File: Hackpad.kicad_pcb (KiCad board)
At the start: 2 copper layers, 21 x 58.5 mm, 4 parts, among them SW1 SW_Push, SW2 SW_Push, SW3 SW_Push, U1 MOUDLE-SEEEDUINO-XIAO

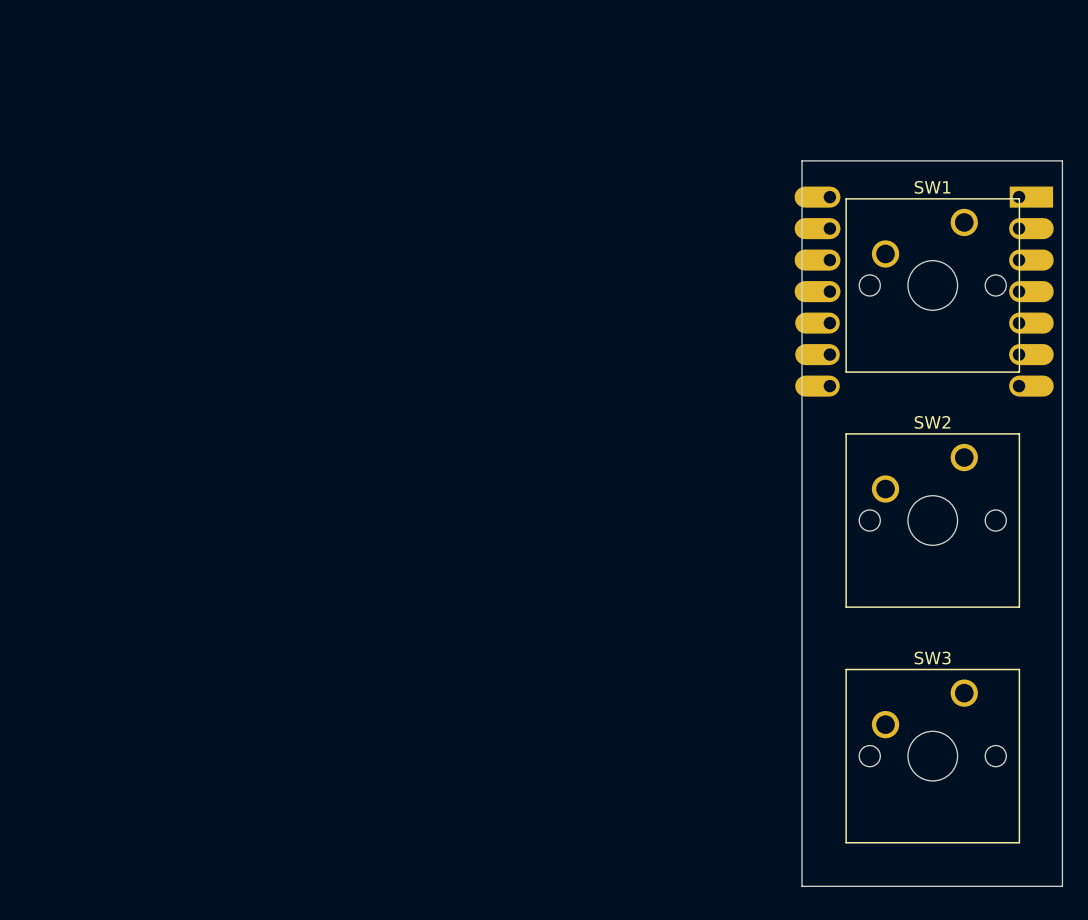
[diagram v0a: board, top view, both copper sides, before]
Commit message: Fixed orioantion of the switches on kicad
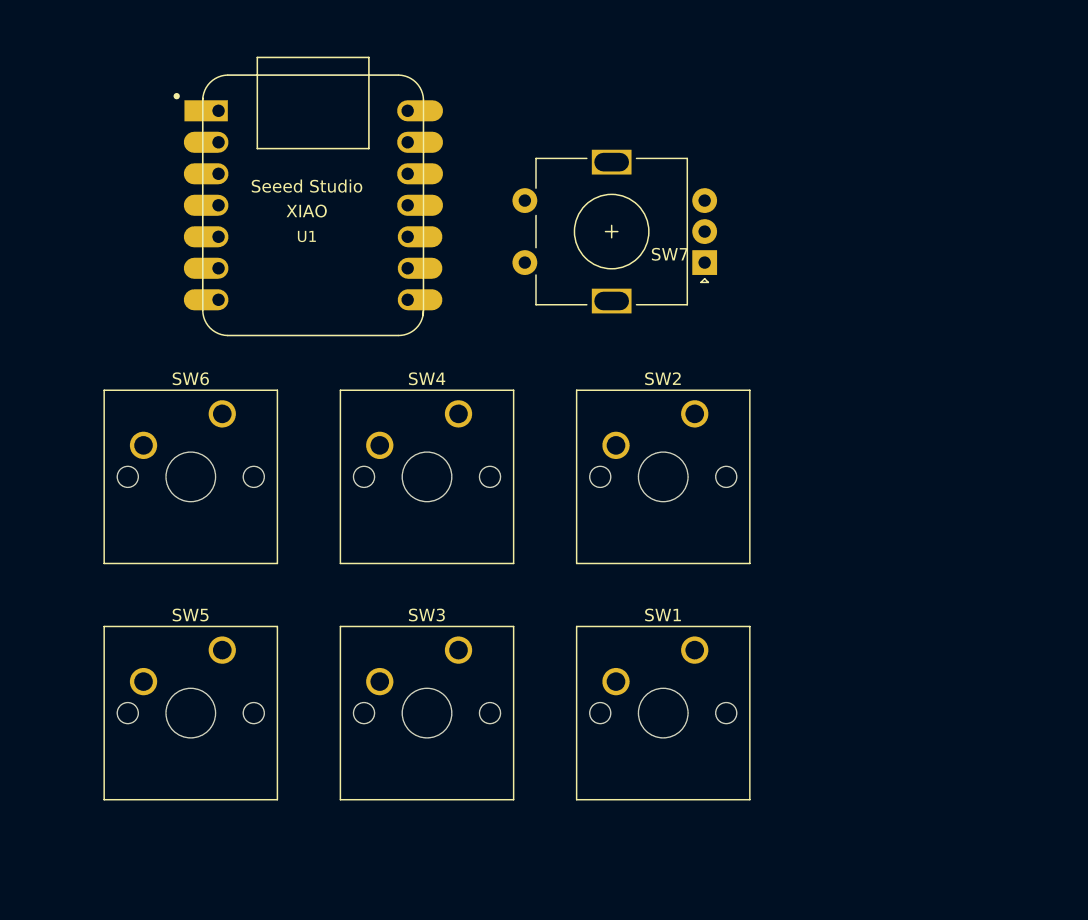
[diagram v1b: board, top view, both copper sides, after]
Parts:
- added SW4: SW_Push, Button_Switch_Keyboard:SW_Cherry_MX_1.00u_PCB, F.Cu at (62.3, 104.4)
- added SW5: SW_Push, Button_Switch_Keyboard:SW_Cherry_MX_1.00u_PCB, F.Cu at (43.2, 123.5)
- added SW6: SW_Push, Button_Switch_Keyboard:SW_Cherry_MX_1.00u_PCB, F.Cu at (43.2, 104.4)
- added SW7: RotaryEncoder_Switch, Rotary_Encoder:RotaryEncoder_Alps_EC11E-Switch_Vertical_H20mm, F.Cu at (82.2, 92.2)
- U1: moved to F.Cu
- moved U1 49.8 mm to (50.6, 87.6), turned to 0 degrees
- moved SW3 40.9 mm to (62.3, 123.5)
- moved SW1 40.8 mm to (81.3, 123.5)
- moved SW2 22.0 mm to (81.3, 104.4)
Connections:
- SW1 pad 1: Net-(U1-PA5_A9_D9_MISO) -> GND
- SW1 pad 2: GND -> Net-(U1-PA02_A0_D0)
- SW2 pad 1: Net-(U1-PA7_A8_D8_SCK) -> GND
- SW2 pad 2: GND -> Net-(U1-PA4_A1_D1)
- SW3 pad 1: Net-(U1-PA6_A10_D10_MOSI) -> GND
- SW3 pad 2: GND -> Net-(U1-PA10_A2_D2)
- U1 pad 1: unconnected-(U1-PA02_A0_D0-Pad1) -> Net-(U1-PA02_A0_D0)
- U1 pad 11: Net-(U1-PA6_A10_D10_MOSI) -> unconnected-(U1-PA6_A10_D10_MOSI-Pad11)
- U1 pad 2: unconnected-(U1-PA4_A1_D1-Pad2) -> Net-(U1-PA4_A1_D1)
- U1 pad 3: unconnected-(U1-PA10_A2_D2-Pad3) -> Net-(U1-PA10_A2_D2)
- U1 pad 4: unconnected-(U1-PA11_A3_D3-Pad4) -> Net-(U1-PA11_A3_D3)
- U1 pad 5: unconnected-(U1-PA8_A4_D4_SDA-Pad5) -> Net-(U1-PA8_A4_D4_SDA)
- U1 pad 6: unconnected-(U1-PA9_A5_D5_SCL-Pad6) -> Net-(U1-PA9_A5_D5_SCL)
- U1 pad 8: unconnected-(U1-PB09_A7_D7_RX-Pad8) -> Net-(U1-PB09_A7_D7_RX)
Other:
- board outline removed

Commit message: added silkscreen art and finished pcb
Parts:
- added G***: LOGO, ZOTEPAD:silk.com.ca.eu.monster.flowerman, F.Cu at (75.1, 86.0)
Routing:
- net GND: track 0.00 -> 156.2 mm, vias 0 -> 2
- net Net-(U1-PA02_A0_D0): track 0.00 -> 59.3 mm
- net Net-(U1-PA10_A2_D2): track 0.00 -> 46.3 mm
- net Net-(U1-PA4_A1_D1): track 0.00 -> 42.2 mm, vias 0 -> 1
- net Net-(U1-PA8_A4_D4_SDA): track 0.00 -> 39.3 mm
- net Net-(U1-PA11_A3_D3): track 0.00 -> 37.7 mm
- net Net-(U1-PB09_A7_D7_RX): track 0.00 -> 32.1 mm
- net Net-(U1-PA7_A8_D8_SCK): track 0.00 -> 24.8 mm
- net Net-(U1-PA9_A5_D5_SCL): track 0.00 -> 17.4 mm
- net Net-(U1-PA5_A9_D9_MISO): track 0.00 -> 10.3 mm, vias 0 -> 1
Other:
- board outline added: 65.3 x 70.1 mm
- board text added: "ZOATBOAT zoat in his boat"
